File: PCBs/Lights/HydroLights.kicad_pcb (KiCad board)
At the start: 2 copper layers, 135.6 x 17.3 mm, 12 parts, among them U1 Solder_Pad, U10 Solder_Pad, U11 Solder_Pad, U2 Solder_Pad, U3 Daylight, U4 Red, U5 Daylight, U6 Blue, U7 Daylight, U8 Green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

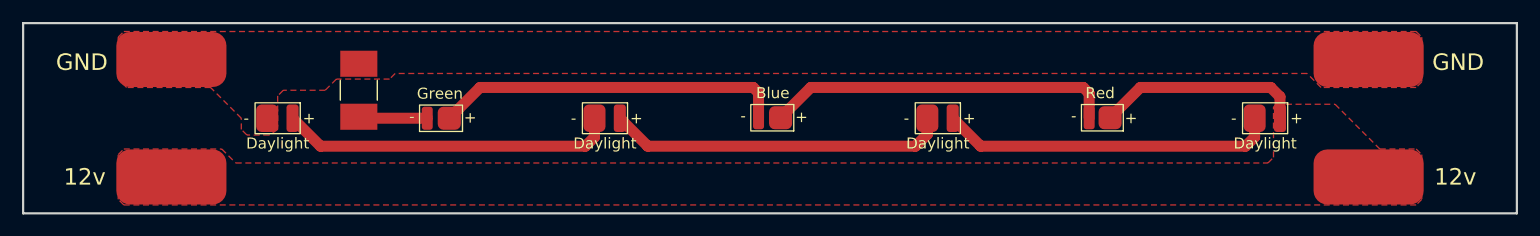
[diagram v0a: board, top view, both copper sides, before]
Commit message: Remove steppers, add OLED
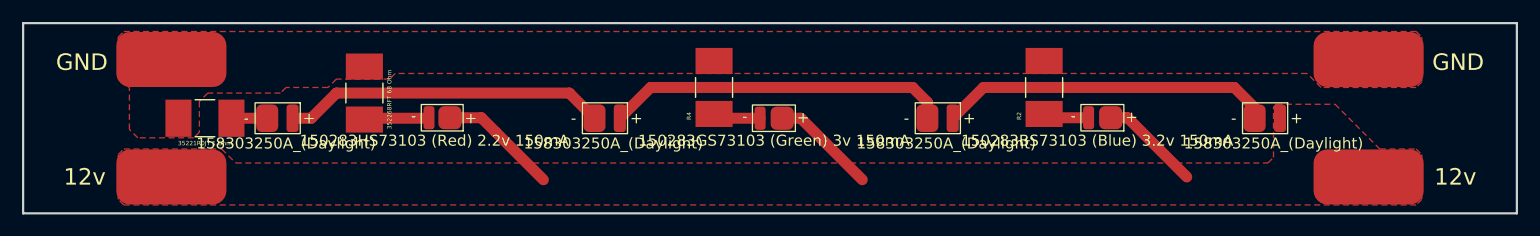
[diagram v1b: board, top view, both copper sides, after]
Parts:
- added R2: 352262RFT 62 Ohm, SnapEDA Library:RESC6332X120N, F.Cu at (161.8, 93.7)
- added R3: 35221R0JT 1 Ohm, SnapEDA Library:RESC6332X120N, F.Cu at (85.6, 96.5)
- added R4: 352262RFT 62 Ohm, SnapEDA Library:RESC6332X120N, F.Cu at (131.8, 93.7)
- R1: value 352216RFT -> 352268RFT 68 Ohm
- U3, U5, U7, U9: value Daylight -> 158303250A_(Daylight)
- U4: value Red -> 150283HS73103 (Red) 2.2v 150mA
- U6: value Blue -> 150283BS73103 (Blue) 3.2v 150mA
- U8: value Green -> 150283GS73103 (Green) 3v 150mA
- moved U4 59.9 mm to (108.9, 97.6)
- moved U8 30.2 mm to (137.2, 96.5)
- moved U6 30.0 mm to (168.9, 97.6)
- moved R1 0.57 mm to (100.1, 94.2)
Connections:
- U4 pad 2: Net-(U4-Pad2) -> Net-(R1-Pad1)
- U6 pad 1: Net-(U4-Pad2) -> 12v
- U6 pad 2: Net-(U6-Pad2) -> Net-(R2-Pad1)
- U8 pad 1: Net-(U6-Pad2) -> 12v
- U8 pad 2: Net-(R1-Pad1) -> Net-(R4-Pad1)
- U9 pad 1: GND -> Net-(R3-Pad2)
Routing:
- net Net-(U6-Pad2): track 31.7 -> 0.00 mm
- net Net-(U4-Pad2): track 31.6 -> 0.00 mm
- net 12v: track 18.9 -> 29.6 mm
- net Net-(R4-Pad1): track 0.00 -> 4.35 mm
- net Net-(R2-Pad1): track 0.00 -> 4.18 mm
- net Net-(R3-Pad2): track 0.00 -> 3.25 mm
- net Net-(U7-Pad1): track 30.5 -> 29.3 mm

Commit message: Finished PCBs
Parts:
- U3, U5, U7, U9: value 158303250A_(Daylight) -> Daylight
- U4: value 150283HS73103 (Red) 2.2v 150mA -> Red
- U6: value 150283BS73103 (Blue) 3.2v 150mA -> Blue
- U8: value 150283GS73103 (Green) 3v 150mA -> Green
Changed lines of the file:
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@@
     (pad_to_mask_clearance 0)
     (pcbplotparams
-      (layerselection 0x00010fc_ffffffff)
+      (layerselection 0x00010f0_ffffffff)
       (disableapertmacros false)
       (usegerberextensions false)
-      (usegerberattributes true)
+      (usegerberattributes false)
       (usegerberadvancedattributes true)
       (creategerberjobfile true)
@@
       (effects (font (size 1 1) (thickness 0.15)))
     )
-    (fp_text value "158303250A_(Daylight)" (at 0.762 2.286 unlocked) (layer "F.SilkS")
+    (fp_text value "Daylight" (at 0.762 2.286 unlocked) (layer "F.SilkS")
       (effects (font (size 1 1) (thickness 0.15)))
     )
@@
       (effects (font (size 1 1) (thickness 0.15)))
     )
-    (fp_text value "158303250A_(Daylight)" (at 0.762 2.286 unlocked) (layer "F.SilkS")
+    (fp_text value "Daylight" (at 0.762 2.286 unlocked) (layer "F.SilkS")
       (effects (font (size 1 1) (thickness 0.15)))
     )
@@
       (effects (font (size 1 1) (thickness 0.15)))
     )
-    (fp_text value "158303250A_(Daylight)" (at 0.762 2.286 unlocked) (layer "F.SilkS")
+    (fp_text value "Daylight" (at 0.762 2.286 unlocked) (layer "F.SilkS")
       (effects (font (size 1 1) (thickness 0.15)))
     )
@@
       (effects (font (size 1 1) (thickness 0.15)))
     )
-    (fp_text value "158303250A_(Daylight)" (at 0.762 2.286 unlocked) (layer "F.SilkS")
+    (fp_text value "Daylight" (at 0.762 2.286 unlocked) (layer "F.SilkS")
       (effects (font (size 1 1) (thickness 0.15)))
     )
@@
       (effects (font (size 0.393701 0.393701) (thickness 0.15)))
     )
-    (fp_text value "352268RFT 68 Ohm" (at -0.59 2.27 90) (layer "F.SilkS")
+    (fp_text value "352268RFT 68 Ohm" (at -0.59 2.27 90) (layer "F.SilkS") hide
       (effects (font (size 0.393701 0.393701) (thickness 0.15)))
     )
@@
       (effects (font (size 1 1) (thickness 0.15)))
     )
-    (fp_text value "150283BS73103 (Blue) 3.2v 150mA" (at 2.313 -0.977 unlocked) (layer "F.SilkS")
+    (fp_text value "Blue" (at 2.313 -0.977 unlocked) (layer "F.SilkS")
       (effects (font (size 1 1) (thickness 0.15)))
     )
@@
       (effects (font (size 1 1) (thickness 0.15)))
     )
-    (fp_text value "150283GS73103 (Green) 3v 150mA" (at -0.1 -2.032 unlocked) (layer "F.SilkS")
+    (fp_text value "Green" (at -0.1 -2.032 unlocked) (layer "F.SilkS")
       (effects (font (size 1 1) (thickness 0.15)))
     )
@@
       (effects (font (size 0.393701 0.393701) (thickness 0.15)))
     )
-    (fp_text value "35221R0JT 1 Ohm" (at 0 2.27) (layer "F.SilkS")
+    (fp_text value "35221R0JT 1 Ohm" (at 0 2.27) (layer "F.SilkS") hide
       (effects (font (size 0.393701 0.393701) (thickness 0.15)))
     )
@@
       (effects (font (size 1 1) (thickness 0.15)))
     )
-    (fp_text value "150283HS73103 (Red) 2.2v 150mA" (at 2.517 -0.977 unlocked) (layer "F.SilkS")
+    (fp_text value "Red" (at 2.517 -0.977 unlocked) (layer "F.SilkS")
       (effects (font (size 1 1) (thickness 0.15)))
     )
@@
     (property "Sheetname" "")
     (attr smd)
-    (fp_text reference "R4" (at -2.59 -2.27 90) (layer "F.SilkS")
-      (effects (font (size 0.393701 0.393701) (thickness 0.15)))
-    )
-    (fp_text value "352262RFT 62 Ohm" (at -0.59 2.27 90) (layer "F.Fab")
+    (fp_text reference "R4" (at -2.59 -2.27 90) (layer "F.SilkS") hide
+      (effects (font (size 0.393701 0.393701) (thickness 0.15)))
+    )
+    (fp_text value "352262RFT 62 Ohm" (at -0.59 2.27 90) (layer "F.Fab") hide
       (effects (font (size 0.393701 0.393701) (thickness 0.15)))
     )
@@
     (property "Sheetname" "")
     (attr smd)
-    (fp_text reference "R2" (at -2.59 -2.27 90) (layer "F.SilkS")
-      (effects (font (size 0.393701 0.393701) (thickness 0.15)))
-    )
-    (fp_text value "352262RFT 62 Ohm" (at -0.59 2.27 90) (layer "F.Fab")
+    (fp_text reference "R2" (at -2.59 -2.27 90) (layer "F.SilkS") hide
+      (effects (font (size 0.393701 0.393701) (thickness 0.15)))
+    )
+    (fp_text value "352262RFT 62 Ohm" (at -0.59 2.27 90) (layer "F.Fab") hide
       (effects (font (size 0.393701 0.393701) (thickness 0.15)))
     )
@@
       (net 1 "GND") (pintype "input"))
   )
-  (gr_rect (start 204.47 88.138) (end 69.342 104.902) (layer "F.Mask") (width 0.15) (fill solid))
   (gr_rect (start 69.088 87.884) (end 204.724 105.156) (layer "Edge.Cuts") (width 0.2) (fill none))
   (gr_text "GND" (at 74.422 91.44) (layer "F.SilkS")
